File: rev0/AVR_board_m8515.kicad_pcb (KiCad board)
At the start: 2 copper layers, 20.3 x 50.8 mm, 18 parts, among them IC1 ATMEGA8515-A, K1 SERIAL, P2 LEFT_HEADER, P3 CONN_3X2, P4 RIGHT_HEADER, P5 EXT_PWR, SW1 RESET_SW, X1 CRYSTAL_TH, X2 CRYSTAL_SMD

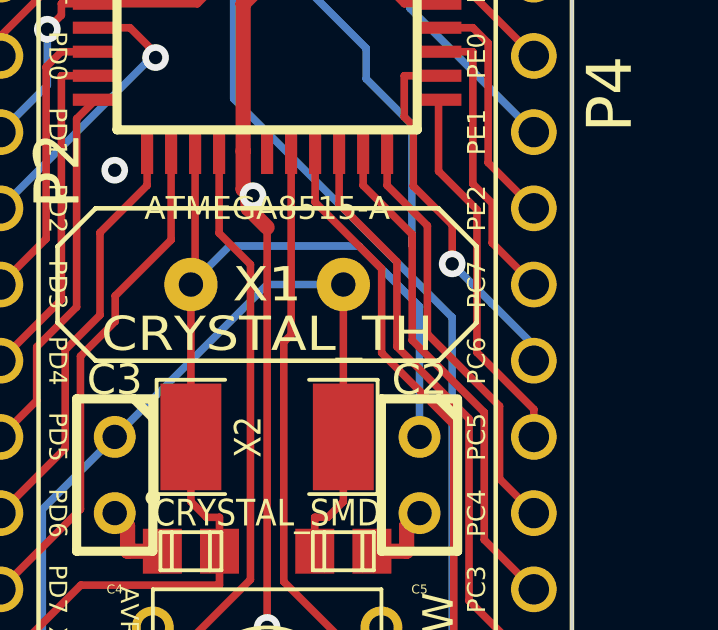
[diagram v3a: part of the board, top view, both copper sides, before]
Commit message: added another GND trace to other GND Plate for niceness
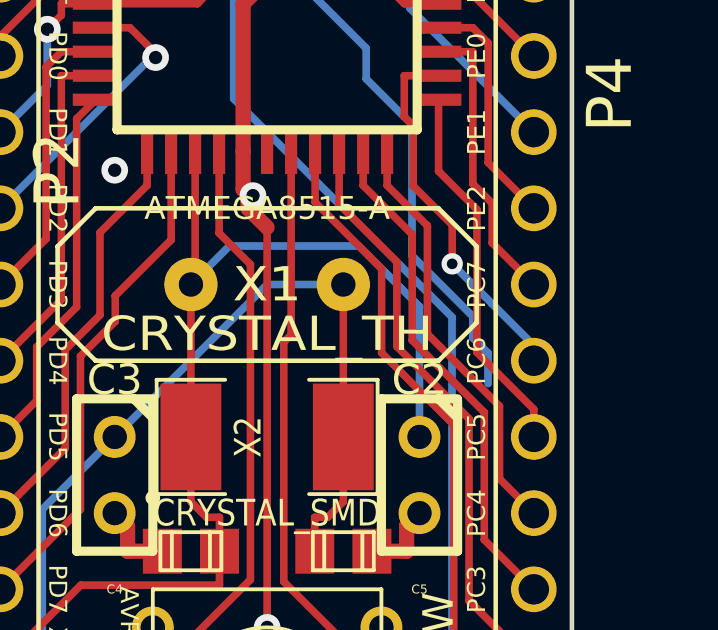
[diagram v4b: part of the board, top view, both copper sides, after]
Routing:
- net GND: track 71.2 -> 76.8 mm
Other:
- net class gnd_stuff: clearance 0.2032 -> 0.1651
- net class smallvia added: clearance 0.254, trace_width 0.254, via_dia 0.7112, via_drill 0.4572
- rule via_min_drill: 0.508 -> 0.381
- rule via_min_size: 0.889 -> 0.6096
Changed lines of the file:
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@@
     (thickness 1.6)
     (drawings 52)
-    (tracks 318)
+    (tracks 323)
     (zones 0)
     (modules 18)
@@
     (via_size 0.889)
     (via_drill 0.635)
-    (via_min_size 0.889)
-    (via_min_drill 0.508)
+    (via_min_size 0.6096)
+    (via_min_drill 0.381)
     (uvia_size 0.508)
     (uvia_drill 0.127)
@@
     (add_net PC4)
     (add_net PC5)
-    (add_net PC6)
     (add_net PC7)
     (add_net PD0)
@@
   )
   (net_class gnd_stuff ""
-    (clearance 0.2032)
+    (clearance 0.1651)
     (trace_width 0.254)
     (via_dia 0.889)
@@
     (uvia_drill 0.127)
     (add_net GND)
+  )
+  (net_class smallvia ""
+    (clearance 0.254)
+    (trace_width 0.254)
+    (via_dia 0.7112)
+    (via_drill 0.4572)
+    (uvia_dia 0.508)
+    (uvia_drill 0.127)
+    (add_net PC6)
   )
   (module C1 (layer F.Cu)
@@
   )
   (via (at 140.97 96.52) (size 0.889) (layers F.Cu B.Cu) (net 0))
+  (segment (start 152.908 102.108) (end 153.416 102.616) (width 0.254) (layer B.Cu) (net 1))
+  (segment (start 150.876 99.362576) (end 152.908 101.394576) (width 0.254) (layer B.Cu) (net 1))
+  (segment (start 152.908 101.394576) (end 152.908 102.108) (width 0.254) (layer B.Cu) (net 1))
   (segment (start 146.558 89.662) (end 146.812 89.916) (width 0.254) (layer F.Cu) (net 1))
   (segment (start 150.876 94.996) (end 150.876 99.06) (width 0.254) (layer B.Cu) (net 1))
@@
   (segment (start 146.812 89.916) (end 149.352 92.456) (width 0.254) (layer B.Cu) (net 1))
   (via (at 146.812 89.916) (size 0.889) (layers F.Cu B.Cu) (net 1))
+  (segment (start 150.876 99.06) (end 150.876 99.362576) (width 0.254) (layer B.Cu) (net 1))
+  (segment (start 153.416 102.616) (end 153.416 103.632) (width 0.254) (layer B.Cu) (net 1))
   (segment (start 150.368 85.852) (end 146.812 85.852) (width 0.254) (layer F.Cu) (net 1))
   (via (at 143.51 86.995) (size 0.889) (layers F.Cu B.Cu) (net 1))
@@
   (segment (start 154.94 104.4884) (end 153.0446 102.593) (width 0.254) (layer F.Cu) (net 25))
   (segment (start 154.94 105.41) (end 154.94 104.4884) (width 0.254) (layer F.Cu) (net 25))
-  (via (at 152.2188 99.6408) (size 0.889) (layers F.Cu B.Cu) (net 26))
+  (via (at 152.2188 99.6408) (size 0.7112) (layers F.Cu B.Cu) (net 26))
   (segment (start 151.765 93.3704) (end 150.6217 93.3704) (width 0.254) (layer F.Cu) (net 26))
   (segment (start 154.94 102.362) (end 153.543 100.965) (width 0.254) (layer B.Cu) (net 26))

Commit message: changed DRC to have some of oshpark's rules
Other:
- rule trace_min: 0.254 -> 0.1524
- rule via_min_drill: 0.381 -> 0.3302
- rule via_min_size: 0.6096 -> 0.508
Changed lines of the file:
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@@
     (zone_clearance 0.508)
     (zone_45_only no)
-    (trace_min 0.254)
+    (trace_min 0.1524)
     (segment_width 0.2)
     (edge_width 0.1)
     (via_size 0.889)
     (via_drill 0.635)
-    (via_min_size 0.6096)
-    (via_min_drill 0.381)
+    (via_min_size 0.508)
+    (via_min_drill 0.3302)
     (uvia_size 0.508)
     (uvia_drill 0.127)

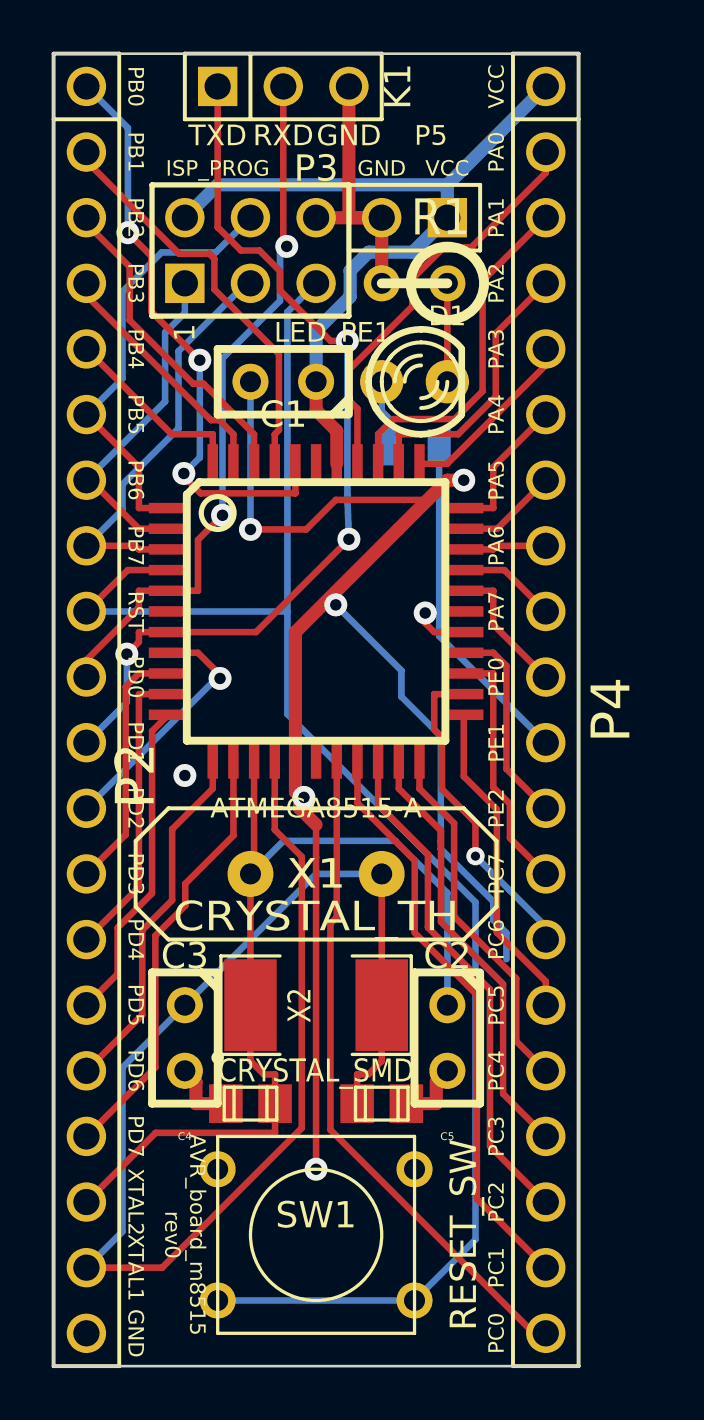
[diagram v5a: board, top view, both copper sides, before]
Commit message: added some gfx, including oshw logo, also did DRC check
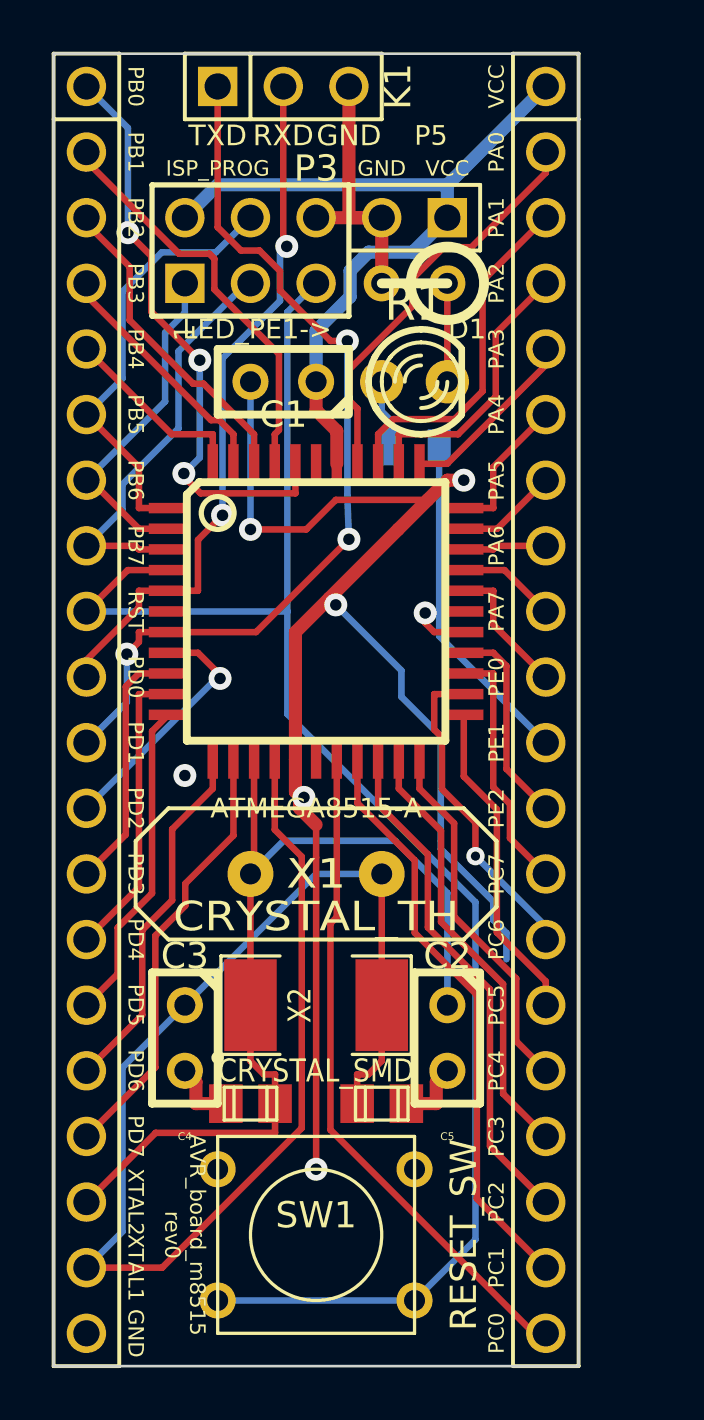
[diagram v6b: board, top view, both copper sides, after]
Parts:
- added G***: LOGO, LOGO, B.Cu at (146.3, 106.2)
- D1: value LED_PE1 -> LED_PE1->
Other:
- board text added: "Designed by: Ethan Durrant/emdarcher"
- board text added: "Open Source Hardware"
- board text added: "https://github.com/emdarcher/AVR_board_m8515"
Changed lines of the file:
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@@
     (links 73)
     (no_connects 0)
-    (area 135.560999 66.8528 158.559 119.709001)
+    (area 128.182143 66.8528 158.559 119.709001)
     (thickness 1.6)
-    (drawings 52)
+    (drawings 55)
     (tracks 323)
     (zones 0)
-    (modules 18)
+    (modules 19)
     (nets 43)
   )
@@
     (descr "LED 3mm - Lead pitch 100mil (2,54mm)")
     (tags "LED led 3mm 3MM 100mil 2,54mm")
-    (fp_text reference D1 (at 1.27 -2.54) (layer F.SilkS)
+    (fp_text reference D1 (at 2.032 -2.032) (layer F.SilkS)
       (effects (font (size 0.762 0.762) (thickness 0.0889)))
     )
-    (fp_text value LED_PE1 (at -3.175 -1.905) (layer F.SilkS)
+    (fp_text value LED_PE1-> (at -6.096 -2.032) (layer F.SilkS)
       (effects (font (size 0.762 0.762) (thickness 0.0889)))
     )
@@
   (module pinarray_20x1 (layer F.Cu)
     (at 137.16 93.98 270)
-    (fp_text reference P2 (at 2.54 -1.905 270) (layer F.SilkS)
+    (fp_text reference P2 (at 2.54 -1.905 270) (layer F.SilkS) hide
       (effects (font (size 1.5 1.5) (thickness 0.15)))
     )
@@
   (module pinarray_20x1 (layer F.Cu)
     (at 154.94 93.98 270)
-    (fp_text reference P4 (at 0 -2.54 270) (layer F.SilkS)
+    (fp_text reference P4 (at 0 -2.54 270) (layer F.SilkS) hide
       (effects (font (size 1.5 1.5) (thickness 0.15)))
     )
@@
     (autoplace_cost90 10)
     (autoplace_cost180 10)
-    (fp_text reference R1 (at -1.016 2.54 180) (layer F.SilkS)
+    (fp_text reference R1 (at 0 -0.762 180) (layer F.SilkS)
       (effects (font (size 1.397 1.27) (thickness 0.2032)))
     )
@@
       (xy 2.71018 0) (xy 2.71018 1.016) (xy 2.71018 2.032) (xy 2.71018 2.032)) (layer B.SilkS) (width 0.00254))
   )
+  (module LOGO (layer B.Cu)
+    (at 146.304 106.172)
+    (fp_text reference G*** (at 0 -5.334) (layer B.SilkS) hide
+      (effects (font (thickness 0.3048)) (justify mirror))
+    )
+    (fp_text value LOGO (at 0 5.334) (layer B.SilkS) hide
+      (effects (font (thickness 0.3048)) (justify mirror))
+    )
+    (fp_poly (pts (xy 5.461 -4.53136) (xy 0.0635 -4.51104) (xy -5.334 -4.48818) (xy -5.35686 0.10414)
+      (xy -5.37718 4.699) (xy -5.3975 0.0635) (xy -5.41782 -4.572) (xy 0.02032 -4.55168)
+      (xy 5.461 -4.53136) (xy 5.461 -4.53136)) (layer B.SilkS) (width 0.00254))
+    (fp_poly (pts (xy 4.572 1.0922) (xy 4.2545 1.14808) (xy 3.86588 1.21666) (xy 3.60934 1.27254)
+      (xy 3.44678 1.34112) (xy 3.34264 1.44272) (xy 3.26136 1.59766) (xy 3.175 1.80848)
+      (xy 2.9718 2.30632) (xy 3.32486 2.80416) (xy 3.67538 3.302) (xy 3.25882 3.72364)
+      (xy 3.04292 3.93446) (xy 2.8702 4.08686) (xy 2.77622 4.14782) (xy 2.77368 4.14782)
+      (xy 2.67462 4.10464) (xy 2.4765 3.99034) (xy 2.24282 3.84048) (xy 1.98628 3.67538)
+      (xy 1.8161 3.59664) (xy 1.68148 3.58902) (xy 1.53416 3.63474) (xy 1.52146 3.63982)
+      (xy 1.34112 3.70332) (xy 1.2446 3.71602) (xy 1.23952 3.71348) (xy 1.20142 3.62712)
+      (xy 1.10998 3.4163) (xy 0.98298 3.10896) (xy 0.83058 2.74066) (xy 0.81788 2.70764)
+      (xy 0.41656 1.73482) (xy 0.63754 1.55702) (xy 0.96012 1.2065) (xy 1.14554 0.80772)
+      (xy 1.19634 0.38862) (xy 1.11252 -0.01778) (xy 0.89916 -0.381) (xy 0.55626 -0.66548)
+      (xy 0.508 -0.69088) (xy 0.08636 -0.83058) (xy -0.3302 -0.82042) (xy -0.7112 -0.67818)
+      (xy -1.0287 -0.42418) (xy -1.25222 -0.07366) (xy -1.35128 0.3556) (xy -1.35382 0.43942)
+      (xy -1.32588 0.82296) (xy -1.21412 1.11252) (xy -0.9906 1.38176) (xy -0.88138 1.48082)
+      (xy -0.59182 1.73482) (xy -0.98044 2.667) (xy -1.13792 3.0353) (xy -1.27762 3.34772)
+      (xy -1.38176 3.5687) (xy -1.4351 3.66522) (xy -1.5494 3.683) (xy -1.72212 3.62966)
+      (xy -1.85674 3.58394) (xy -1.99136 3.59664) (xy -2.16916 3.683) (xy -2.41046 3.83794)
+      (xy -2.65938 3.99542) (xy -2.85242 4.10718) (xy -2.94386 4.14782) (xy -3.03276 4.09194)
+      (xy -3.20294 3.94462) (xy -3.41884 3.73634) (xy -3.429 3.72618) (xy -3.84302 3.302)
+      (xy -3.49504 2.79654) (xy -3.14452 2.28854) (xy -3.36042 1.78562) (xy -3.48488 1.51384)
+      (xy -3.58648 1.3589) (xy -3.71094 1.28016) (xy -3.8989 1.23952) (xy -3.97002 1.22936)
+      (xy -4.3307 1.17602) (xy -4.55676 1.12268) (xy -4.68122 1.03886) (xy -4.73202 0.89154)
+      (xy -4.74218 0.65024) (xy -4.74218 0.45974) (xy -4.74218 -0.16256) (xy -4.42468 -0.25146)
+      (xy -4.15544 -0.30988) (xy -3.91668 -0.34036) (xy -3.89382 -0.34036) (xy -3.70078 -0.36068)
+      (xy -3.56108 -0.4445) (xy -3.43916 -0.61976) (xy -3.30454 -0.90678) (xy -3.11658 -1.3462)
+      (xy -3.47726 -1.86182) (xy -3.84048 -2.37998) (xy -3.3909 -2.83464) (xy -2.93878 -3.29184)
+      (xy -2.39268 -2.92354) (xy -1.84658 -2.55778) (xy -1.4097 -2.75844) (xy -0.97282 -2.9591)
+      (xy -0.85344 -3.59918) (xy -0.73152 -4.2418) (xy -0.09652 -4.2164) (xy 0.54102 -4.191)
+      (xy 0.6731 -3.56616) (xy 0.80518 -2.94132) (xy 1.2446 -2.74828) (xy 1.68402 -2.55524)
+      (xy 2.21742 -2.92862) (xy 2.75082 -3.29946) (xy 3.20548 -2.84734) (xy 3.66014 -2.39268)
+      (xy 3.30454 -1.86944) (xy 2.95148 -1.3462) (xy 3.14198 -0.88646) (xy 3.25628 -0.62738)
+      (xy 3.37058 -0.47244) (xy 3.53314 -0.38354) (xy 3.79222 -0.32512) (xy 3.937 -0.29972)
+      (xy 4.2545 -0.24638) (xy 4.44246 -0.18542) (xy 4.53644 -0.07366) (xy 4.56946 0.127)
+      (xy 4.572 0.45466) (xy 4.572 0.46736) (xy 4.572 1.0922) (xy 4.572 1.0922)) (layer B.SilkS) (width 0.00254))
+  )
+  (gr_text "Open Source\nHardware" (at 146.304 110.744) (layer B.SilkS)
+    (effects (font (size 0.8 0.8) (thickness 0.2)) (justify mirror))
+  )
+  (gr_text https://github.com/emdarcher/AVR_board_m8515 (at 139.7 89.916 90) (layer B.SilkS)
+    (effects (font (size 0.6 0.6) (thickness 0.15)) (justify mirror))
+  )
+  (gr_text "Designed by:\nEthan Durrant/emdarcher" (at 146.304 96.52) (layer B.SilkS)
+    (effects (font (size 0.6 0.6) (thickness 0.15)) (justify mirror))
+  )
   (gr_line (start 135.89 119.38) (end 135.89 68.58) (angle 90) (layer Edge.Cuts) (width 0.1))

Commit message: generated gerber and drill file, must check though
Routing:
- net GND: track 76.8 -> 78.9 mm
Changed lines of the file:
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@@
     (thickness 1.6)
     (drawings 55)
-    (tracks 323)
+    (tracks 325)
     (zones 0)
     (modules 19)
@@
     (visible_elements FFFFFF7F)
     (pcbplotparams
-      (layerselection 3178497)
+      (layerselection 284196865)
       (usegerberextensions true)
       (excludeedgelayer true)
@@
       (outputformat 1)
       (mirror false)
-      (drillshape 1)
+      (drillshape 0)
       (scaleselection 1)
       (outputdirectory ""))
@@
   )
   (via (at 140.97 96.52) (size 0.889) (layers F.Cu B.Cu) (net 0))
+  (segment (start 139.192 118.364) (end 137.414 118.364) (width 0.254) (layer B.Cu) (net 1) (status 800000))
+  (segment (start 137.414 118.364) (end 137.16 118.11) (width 0.254) (layer B.Cu) (net 1) (status C00000))
   (segment (start 152.908 102.108) (end 153.416 102.616) (width 0.254) (layer B.Cu) (net 1))
   (segment (start 150.876 99.362576) (end 152.908 101.394576) (width 0.254) (layer B.Cu) (net 1))
